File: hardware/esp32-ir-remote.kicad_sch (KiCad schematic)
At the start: 65 parts, among them J1 ESP32-WROOM-32E-Breakout, J2 USB_C_Receptacle_USB2.0_14P, Q1 Q_NPN_BCE, Q2 Q_NPN_BCE, Q3 IRLML6344, Q4 2N7002, Q5 2N7002, SW1 RESET, SW2 BOOT, U1 AP63203WU, U2 CH340C, U3 ESP32-WROOM-32E, U4 TSOP382xx, U5 AM2302

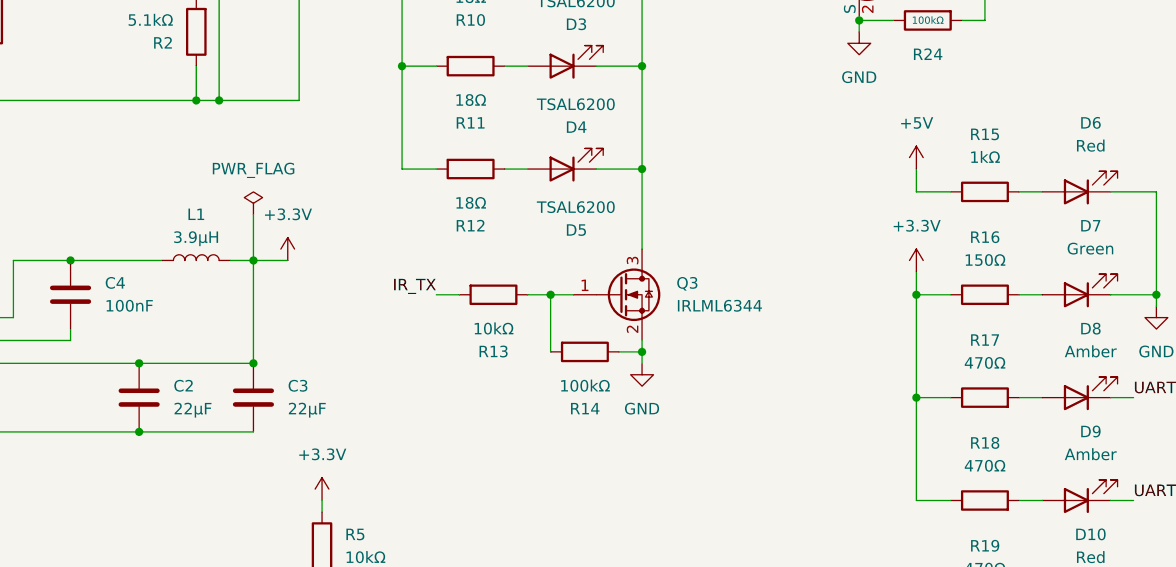
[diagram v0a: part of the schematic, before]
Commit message: v1.2 Tier 1: H1.4 value fixes + LCSC backfill (via kicad-edit MCP, netlist-verified)
Values: R13 gate resistor 10k->470R (38kHz IR switching speed), L1
3.9uH->4.7uH (SWPA6045S4R7MT C78804: Isat 5.5A, DCR 26mOhm, 6x6mm; no
Basic-library 4.7uH power inductor exists anymore - SWPA series moved to
Extended, accepted one feeder fee), R16 D7-green 150R->470R (consolidates
with R17-R19).

LCSC backfill on the 15 H1.2 gap parts (C10, D1, D4-D12, F1, SW1, SW2)
function-matched per the ROADMAP table. Also FIXED a latent BOM bug found
during census: R13/R22 (10k) carried C17955 - the 18-ohm code from the
R9-R12 group; R22 corrected to C17414 matching R3-R8.

Netlist diff verified: fields/values only, nets section untouched. ERC
report unchanged vs committed baseline (1 expected error + 5 warnings;
ROADMAP's '9 violations' baseline note was stale).
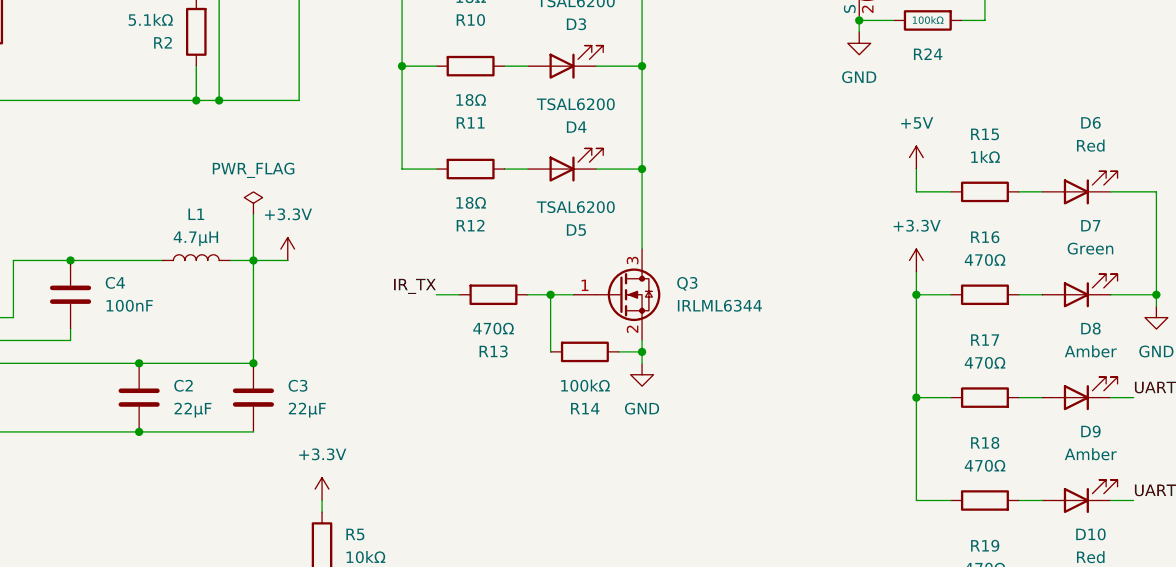
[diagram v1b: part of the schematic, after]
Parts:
- C10: LCSC (none) -> C14663
- D1: LCSC (none) -> C83333
- D10, D6: LCSC (none) -> C99772
- D11, D12: LCSC (none) -> C86881
- D4, D5: LCSC (none) -> C55528
- D7: LCSC (none) -> C85161
- D8, D9: LCSC (none) -> C85160
- F1: LCSC (none) -> C142747
- L1: value 3.9µH -> 4.7µH; LCSC (none) -> C78804
- R13: value 10kΩ -> 470Ω; LCSC C17955 -> C17710
- R16: value 150Ω -> 470Ω; LCSC C17471 -> C17710
- R22: LCSC C17955 -> C17414
- SW1, SW2: LCSC (none) -> C455280
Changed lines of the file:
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@@
 			)
 		)
+    (property "LCSC" "C55528" (at 205.74 73.66 0)
+      (effects (font (size 1.27 1.27)) (hide yes))
+    )
 		(pin "1"
 		)
@@
 			)
 		)
+    (property "LCSC" "C99772" (at 262.89 121.92 0)
+      (effects (font (size 1.27 1.27)) (hide yes))
+    )
 		(pin "1"
 		)
@@
 			)
 		)
+    (property "LCSC" "C83333" (at 176.53 36.83 0)
+      (effects (font (size 1.27 1.27)) (hide yes))
+    )
 		(pin "1"
 		)
@@
 			)
 		)
+    (property "LCSC" "C85160" (at 262.89 99.06 0)
+      (effects (font (size 1.27 1.27)) (hide yes))
+    )
 		(pin "1"
 		)
@@
 			)
 		)
+    (property "LCSC" "C455280" (at 259.08 153.67 0)
+      (effects (font (size 1.27 1.27)) (hide yes))
+    )
 		(pin "2"
 		)
@@
 			)
 		)
-		(property "Value" "150Ω"
+		(property "Value" "470Ω"
 			(at 252.73 83.82 90)
 			(effects
@@
 			)
 		)
-		(property "LCSC" "C17471"
+		(property "LCSC" "C17710"
 			(at 252.73 87.63 0)
 			(effects
@@
 			)
 		)
+    (property "LCSC" "C99772" (at 262.89 76.2 0)
+      (effects (font (size 1.27 1.27)) (hide yes))
+    )
 		(pin "1"
 		)
@@
 			)
 		)
+    (property "LCSC" "C86881" (at 232.41 45.72 0)
+      (effects (font (size 1.27 1.27)) (hide yes))
+    )
 		(pin "1"
 		)
@@
 			)
 		)
+    (property "LCSC" "C455280" (at 259.08 142.24 0)
+      (effects (font (size 1.27 1.27)) (hide yes))
+    )
 		(pin "2"
 		)
@@
 			)
 		)
+    (property "LCSC" "C14663" (at 105.41 121.92 0)
+      (effects (font (size 1.27 1.27)) (hide yes))
+    )
 		(pin "1"
 		)
@@
 			)
 		)
-		(property "Value" "3.9µH"
+		(property "Value" "4.7µH"
 			(at 165.1 81.28 90)
 			(effects
@@
 			)
 		)
+    (property "LCSC" "C78804" (at 165.1 83.82 0)
+      (effects (font (size 1.27 1.27)) (hide yes))
+    )
 		(pin "2"
 		)
@@
 			)
 		)
+    (property "LCSC" "C85160" (at 262.89 110.49 0)
+      (effects (font (size 1.27 1.27)) (hide yes))
+    )
 		(pin "1"
 		)
@@
 			)
 		)
+    (property "LCSC" "C85161" (at 262.89 87.63 0)
+      (effects (font (size 1.27 1.27)) (hide yes))
+    )
 		(pin "1"
 		)
@@
 			)
 		)
+    (property "LCSC" "C86881" (at 241.3 29.21 0)
+      (effects (font (size 1.27 1.27)) (hide yes))
+    )
 		(pin "1"
 		)
@@
 			)
 		)
+    (property "LCSC" "C55528" (at 205.74 62.23 0)
+      (effects (font (size 1.27 1.27)) (hide yes))
+    )
 		(pin "1"
 		)
@@
 			)
 		)
-		(property "Value" "10kΩ"
+		(property "Value" "470Ω"
 			(at 198.12 91.44 90)
 			(effects
@@
 			)
 		)
-		(property "LCSC" "C17955"
+		(property "LCSC" "C17710"
 			(at 198.12 87.63 0)
 			(effects
@@
 			)
 		)
-		(property "LCSC" "C17955"
+		(property "LCSC" "C17414"
 			(at 161.29 168.91 0)
 			(effects
@@
 			)
 		)
+    (property "LCSC" "C142747" (at 157.48 26.67 0)
+      (effects (font (size 1.27 1.27)) (hide yes))
+    )
 		(pin "1"
 		)

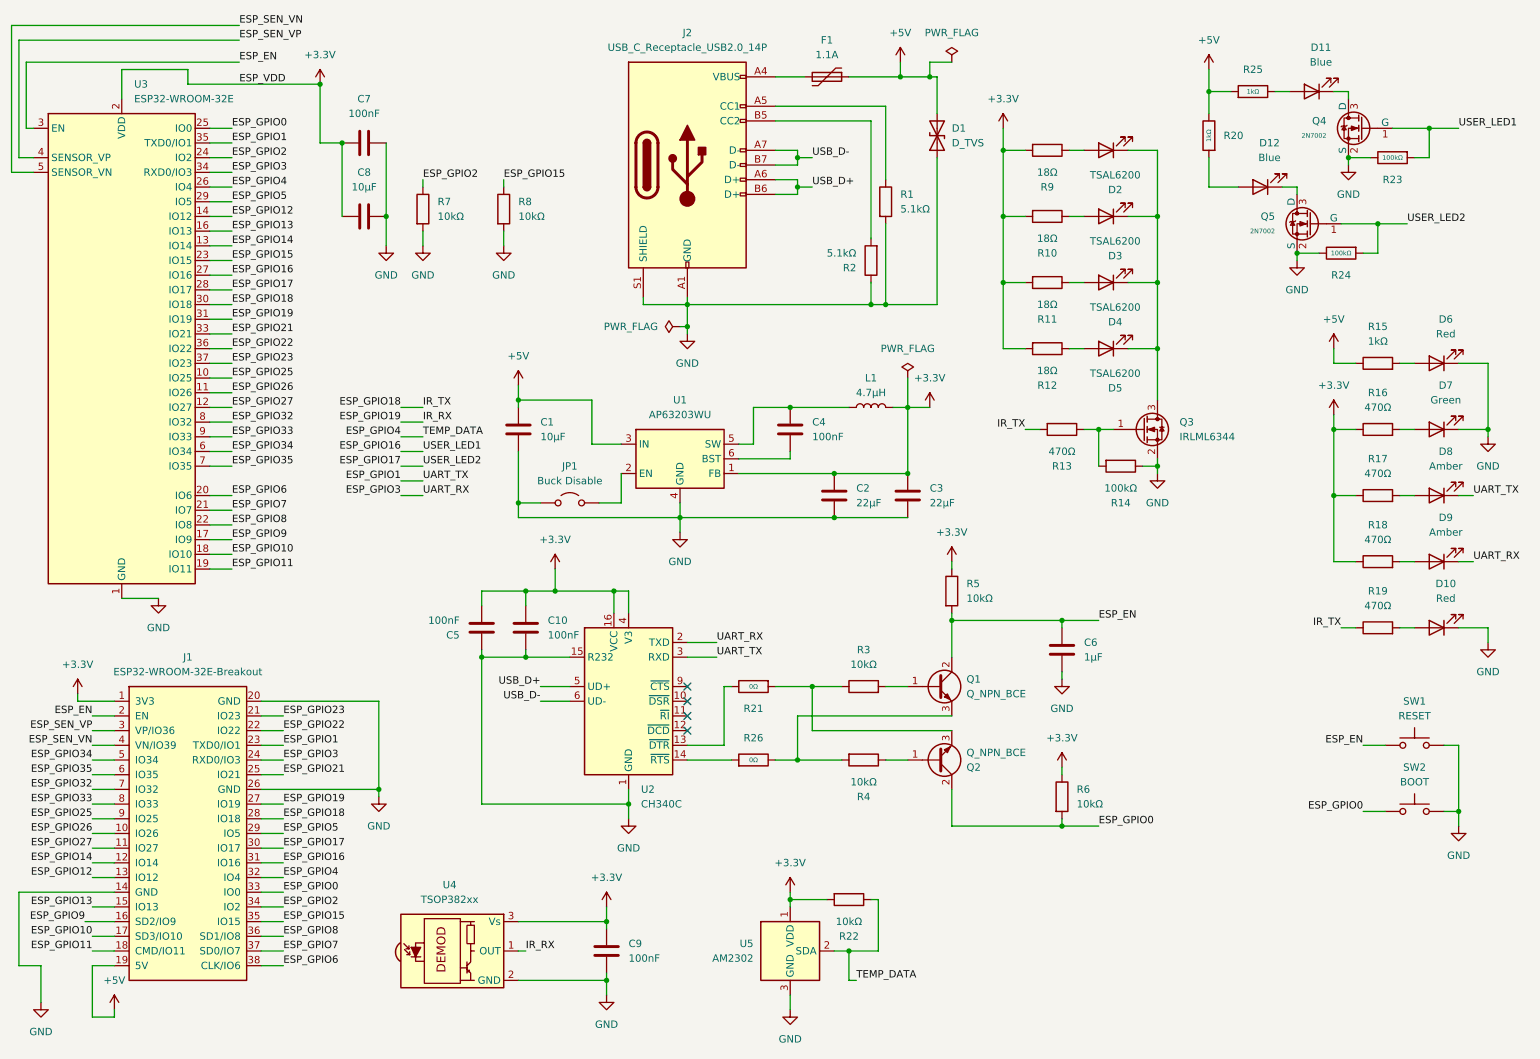
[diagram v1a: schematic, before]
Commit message: v1.2: standardize 8 PCM_JLCPCB symbols to generic libs (electrically empty)
R20/R21/R23-R26 -> Device:R, Q4/Q5 -> Transistor_FET:Q_NMOS_GSD; footprints
PCM_JLCPCB:* -> Resistor_SMD / Package_TO_SOT_SMD:SOT-23. Removes the last
dependency on the third-party PCM_JLCPCB plugin libs.

Gotchas found and fixed during the swap (kicad-edit MCP lessons):
- The PCM NMOS symbol is the MIRROR of Q_NMOS_GSD: a naive replace left
  Q4/Q5 pins floating in air. Fixed with (mirror y) on both instances -
  all three pins land exactly on the original wire endpoints.
- replace_schematic_component resets Datasheet to '~'; restored all 8 URLs.
- The MCP rewrite perturbed the embedded USB-C lib symbol (new
  lib_symbol_mismatch warning on J2); spliced the HEAD version back.

Verified: net partition identical to HEAD (machine-checked pin-by-pin);
ERC back to baseline 6 (1 expected FLG03 error + 5 dual-label warnings).
Cosmetic: 4 auto-named LED-driver nets renamed to unconnected-(D11/D12-*)
by the netlister; connectivity unaffected, will normalize in H1.3.
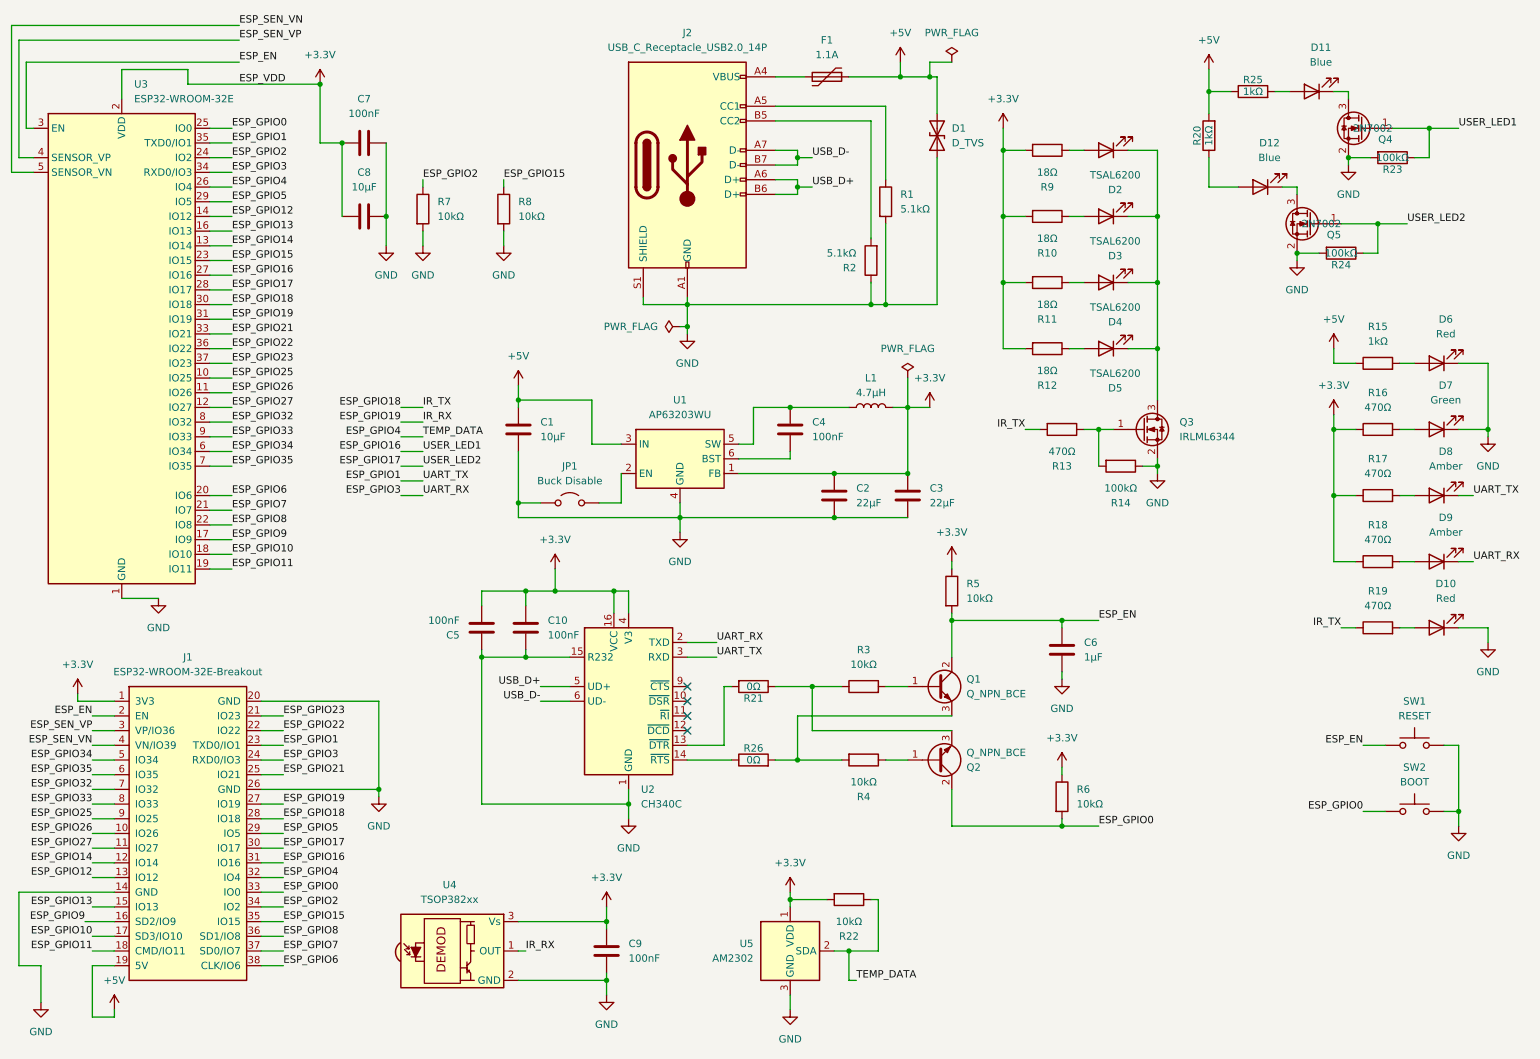
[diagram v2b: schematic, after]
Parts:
- removed Q4, Q5: 2N7002, PCM_JLCPCB:Q_SOT-23, symbol PCM_JLCPCB-Transistors:NMOS,2N7002
- removed R20, R25: 1kΩ, PCM_JLCPCB:R_0805, symbol PCM_JLCPCB-Resistors:0805,1kΩ
- removed R21, R26: 0Ω, PCM_JLCPCB:R_0603, symbol PCM_JLCPCB-Resistors:0603,0Ω
- removed R23, R24: 100kΩ, PCM_JLCPCB:R_0603, symbol PCM_JLCPCB-Resistors:0603,100kΩ
- added Q4, Q5: 2N7002, Package_TO_SOT_SMD:SOT-23, symbol Transistor_FET:Q_NMOS_GSD
- added R20, R25: 1kΩ, Resistor_SMD:R_0805_2012Metric, symbol Device:R
- added R21, R26: 0Ω, Resistor_SMD:R_0603_1608Metric, symbol Device:R
- added R23, R24: 100kΩ, Resistor_SMD:R_0603_1608Metric, symbol Device:R
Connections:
- net +5V: now also R20.2, R25.1
- net ESP_GPIO16: now also Q4.1 (G), R23.1
- net ESP_GPIO17: now also Q5.1 (G), R24.1
- net GND: now also Q4.2 (S), Q5.2 (S), R23.2, R24.2
- net at Q2.3 (E), R3.1: now also R21.1
- net at Q1.3 (E), R4.2: now also R26.2
- net at D12.1 (K): now also Q5.3 (D)
- net at D12.2 (A): now also R20.1
- net at U2.14 (~{RTS}): now also R26.1
- net at U2.13 (~{DTR}): now also R21.2
- net at D11.1 (K): now also Q4.3 (D)
- net at D11.2 (A): now also R25.2
